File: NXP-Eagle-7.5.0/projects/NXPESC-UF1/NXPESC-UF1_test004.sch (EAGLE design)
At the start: 88 parts, among them J1 ARM_MINI_JTAG-TH, P1 MOT_PWR_PAD-1, P15 DF13-6P-1.25H, P18 DF13-5P-1.25H, P2 MOT_PWR_PAD-1, P3 MOT_PWR_PAD-1, P4 MOT_PWR_PAD-1, P5 MOT_PWR_PAD-1, P8 DF13-4P-1.25H, P9 DF13-4P-1.25H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

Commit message: revisions. Adding MCU components, ESD protection, Thermister, oscillator, RGB LED, checking pinout. Moved CAN interface connection.
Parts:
- added C23, C24, C25, C26, C30: CAP0603-0.1UF-25V, etc-rcl:CAP0603-0.1UF-25V
- added C27, C29: CAP0603-2.2NF-25V, etc-rcl:CAP0603-2.2NF-25V
- added C28, C31: CAP0603-15PF, etc-rcl:CAP0603-15PF
- added D4: CLV1A-FKB, CLV1A-FKB:CLV1A-FKB
- added D5: PESD1CAN, PESD1CAN:PESD1CAN
- added R32, R33: RESC0603-100R, etc-rcl:RESC0603-100R
- added R34: RESC0603-1K-1, etc-rcl:RESC0603-1K-1
- added R35, R40: RESC0603-10K-1, etc-rcl:RESC0603-10K-1
- added R36, R37: RESC0603-270K-1, etc-rcl:RESC0603-270K-1
- added R38, R41: RESC0603-4.99K-1, etc-rcl:RESC0603-4.99K-1
- added R43: RESC0603-576R-1, etc-rcl:RESC0603-576R-1
- added SH2, SH3: RESC0603-0R, etc-rcl:RESC0603-0R
- added U24: DF13-2P-1.25H, pixhawk2:DF13-2P-1.25H
- added Y1: ABM3B-8.000MHZ-B2-T, ABM3B-8.000MHZ-B2-T:ABM3B-8.000MHZ-B2-T
- C1, C20, C21, C22: value CAP0603-1UF-50V -> CAP0603-0.1UF-50V; device etc-rcl:CAP0603-1UF-50V -> etc-rcl:CAP0603-0.1UF-50V
- R42: value (none) -> RESC0603-10K-1; device pixhawk2:RESISTOR0402-RES -> etc-rcl:RESC0603-10K-1
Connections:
- net N$25 renamed ENC_A_X
- net N$26 renamed ENC_B_X
- net N$27 renamed ENC_I_X
- net N$29 renamed ENC_A_IN
- net N$32 renamed ENC_B_IN
- net N$35 renamed ENC_I_IN
- removed net ENC_C: U1.~O5
- new net ADC1_DM1: C27.1, R33.1, U2.PTE19
- new net ADC1_DP1: C29.1, R32.1, U2.PTE18
- new net ENC_I: U1.~O5, U2.PTA13/LLWU_P4
- new net EXTAL0: C28.1, U2.PTA18, Y1.1
- new net LEDRGB-BLU/PTE25: R37.2, U2.PTD3
- new net LEDRGB-GRN/PTD7: R36.2, U2.PTD7
- new net LEDRGB-RED/PTD1: R43.2, U2.PTD1
- new net N$25: D4.A, R42.2
- new net N$26: C30.2, R33.2, R41.2, U24-2.S
- new net N$27: C30.1, R32.2, R38.2, U24-1.S
- new net N$28: D4.CBLUE, R37.1
- new net N$29: D4.CGREEN, R36.1
- new net N$30: D4.CRED, R43.1
- new net N$31: SH3.2, U2.VDDA, U2.VREFH
- new net N$32: SH2.2, U2.VREFL, U2.VSSA
- new net N$8: U2.PTB1
- new net VOLT_DCB/ADC0_SE13: C24.1, R34.2, R35.1, U2.PTB3
- new net XTAL0: C31.1, U2.PTA19, Y1.2
- net +3V3: now also C23.1, C26.1, R38.1, R42.1, SH3.1, U1.VCC
- net +5V: now also C25.1; no longer U1.VCC
- net +V_MOTOR: now also R35.2
- net AGND: now also R34.1
- net CAN0_RX: now also U2.PTE25; no longer U2.PTA13/LLWU_P4
- net CAN0_TX: now also U2.PTE24; no longer U2.PTA12
- net CANH: now also D5.1
- net CANL: now also D5.2
- net GND: now also C23.2, C24.2, C25.2, C26.2, C27.2, C28.2, C29.2, C31.2, D5.3, R41.1, SH2.1, Y1.GND
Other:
- note added: "*Values TBD. Compare with FRDM-MC-LVPMSM"
- note added: "10K Thermister Vdiff ~0.372V to 2.879V (Ta=25C 1.650V)"
- note added: "8Mhz or 16Mhz?"
- note added: "Add 10uH inductor"
- note added: "DCB Voltage Sense"
- note added: "Encoder C needs a home. Currently taken by CANRX! (should be Quadrature input)"
- note added: "Is external XTAL needed for FOC ESC?"
- note added: "Likely possible to remove RC?"
- note added: "Optional: Encoder input (Separate mezzanine board)"
- note added: "PTB1/FTM1_CH1/FTM1_QD_PHB"
- note added: "PTD3 Pin arbitrarily picked. Was PTE25"
- note added: "PTE24/CAN0_TX"
- note added: "PTE25/CAN0_RX"
- note added: "RGB LED"
- note added: "Thermister Input"
- note added: "Thermister input"
- note added: "replace w SMT 10uH inductors/bead"
- note removed: "Encoder C needs a home. Currently taken by CANRX!"
- moved on the sheet: CA1, J1-GND1, J1-GND2, J1-GND3, J1-TCK/SWCLK, J1-TDI/EXTB, J1-TDO/SWO, J1-TMS/SWDIO, J1-VTREF, J1-~{RESET}, P18-1, P18-2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

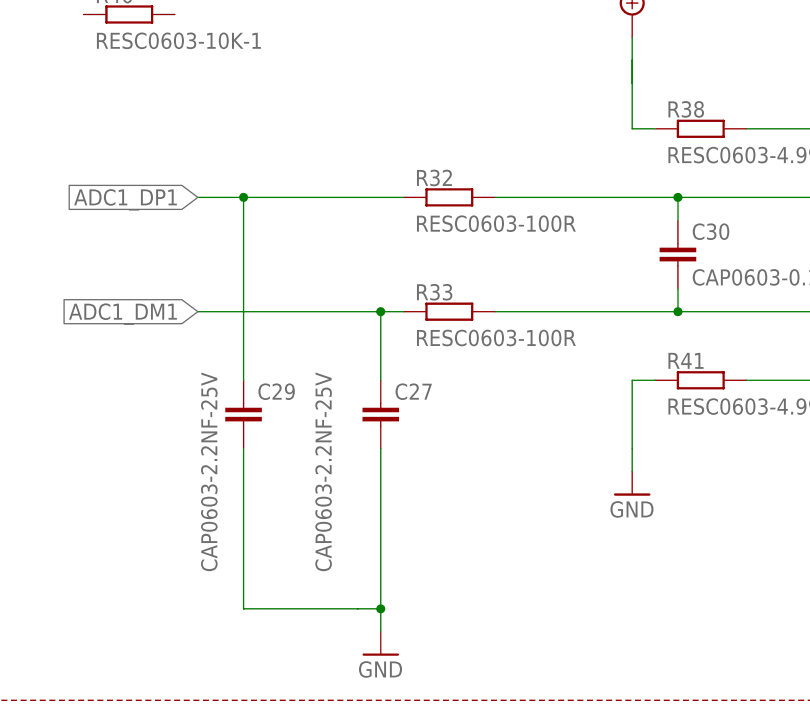
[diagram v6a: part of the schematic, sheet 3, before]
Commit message: Placing all new parts from schematic update. Looks tricky to fit everything onto this size board. Will likely need to make a bit bigger.
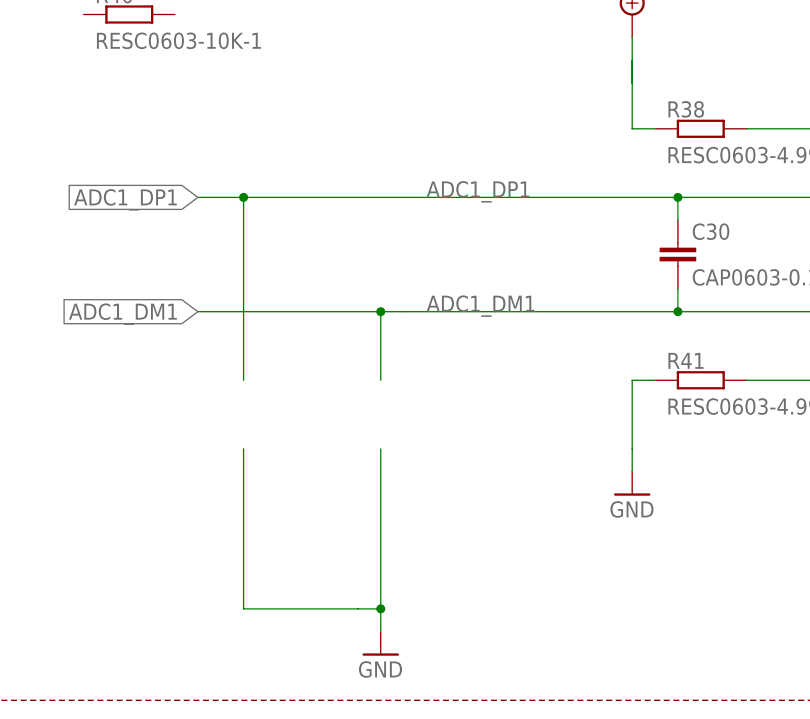
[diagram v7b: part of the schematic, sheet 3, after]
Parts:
- removed C27, C29: CAP0603-2.2NF-25V, etc-rcl:CAP0603-2.2NF-25V
- removed R32, R33: RESC0603-100R, etc-rcl:RESC0603-100R
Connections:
- removed net N$26: C30.2, R33.2, R41.2, U24-2.S
- removed net N$27: C30.1, R32.2, R38.2, U24-1.S
- net ADC1_DM1: now also C30.2, R41.2, U24-2.S; no longer C27.1, R33.1
- net ADC1_DP1: now also C30.1, R38.2, U24-1.S; no longer C29.1, R32.1
- net GND: no longer C27.2, C29.2
